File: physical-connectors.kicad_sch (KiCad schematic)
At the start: 2 parts, among them J1 M.2_Key_B

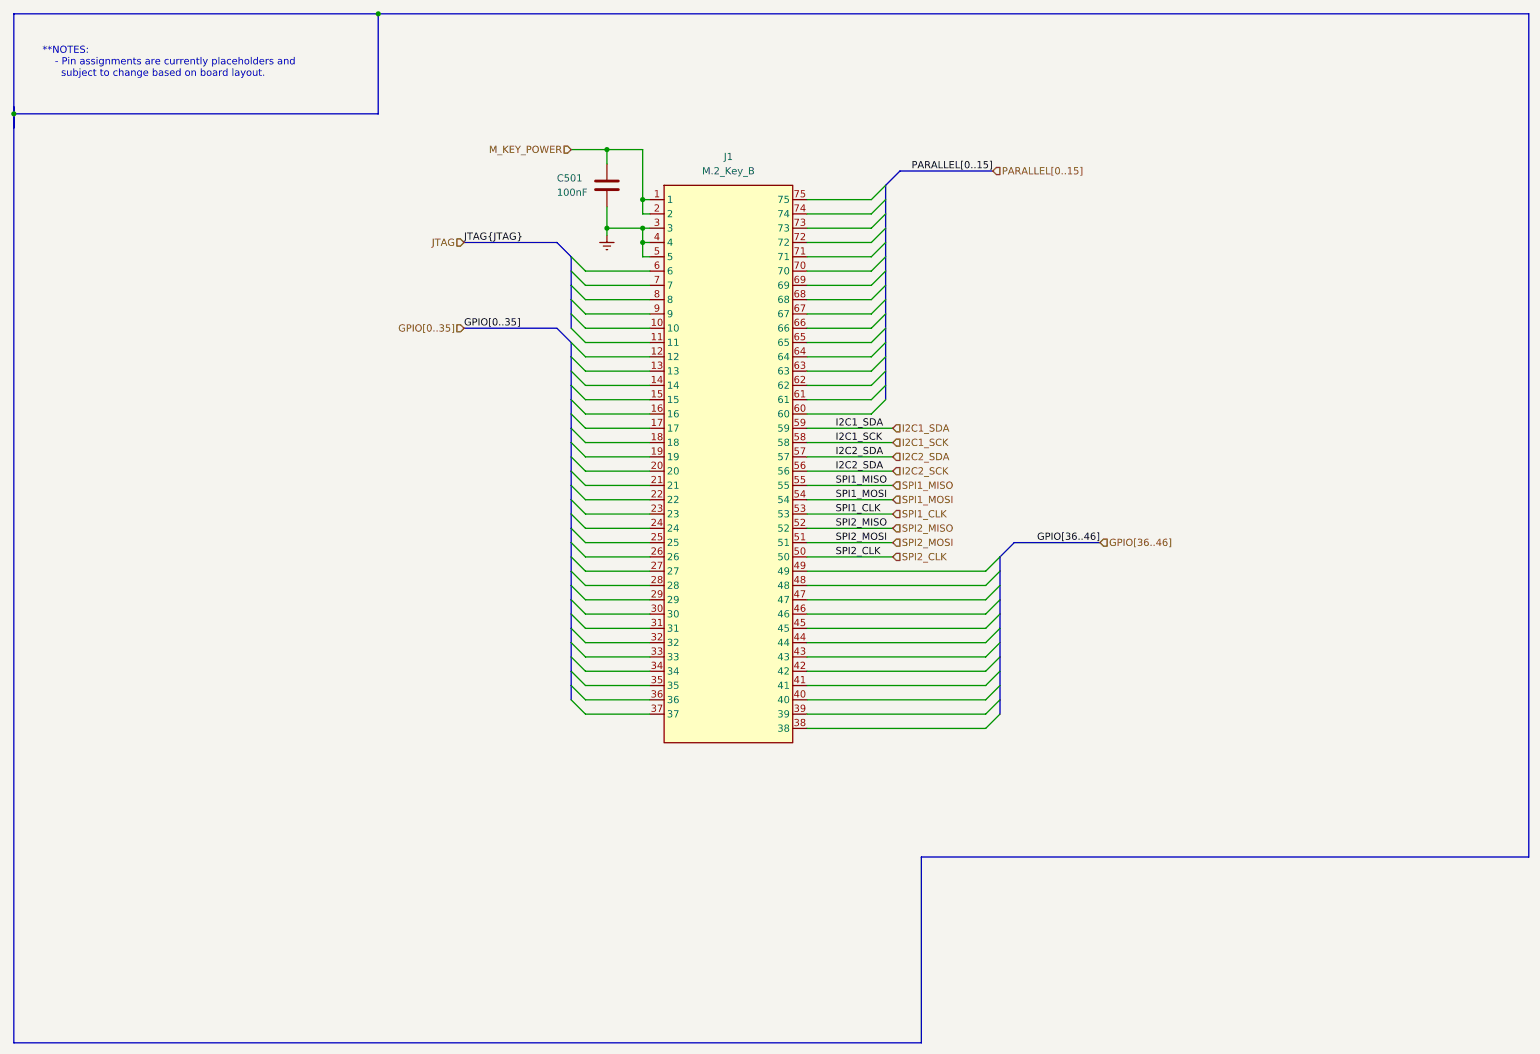
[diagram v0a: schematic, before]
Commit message: added net labels; changed colours
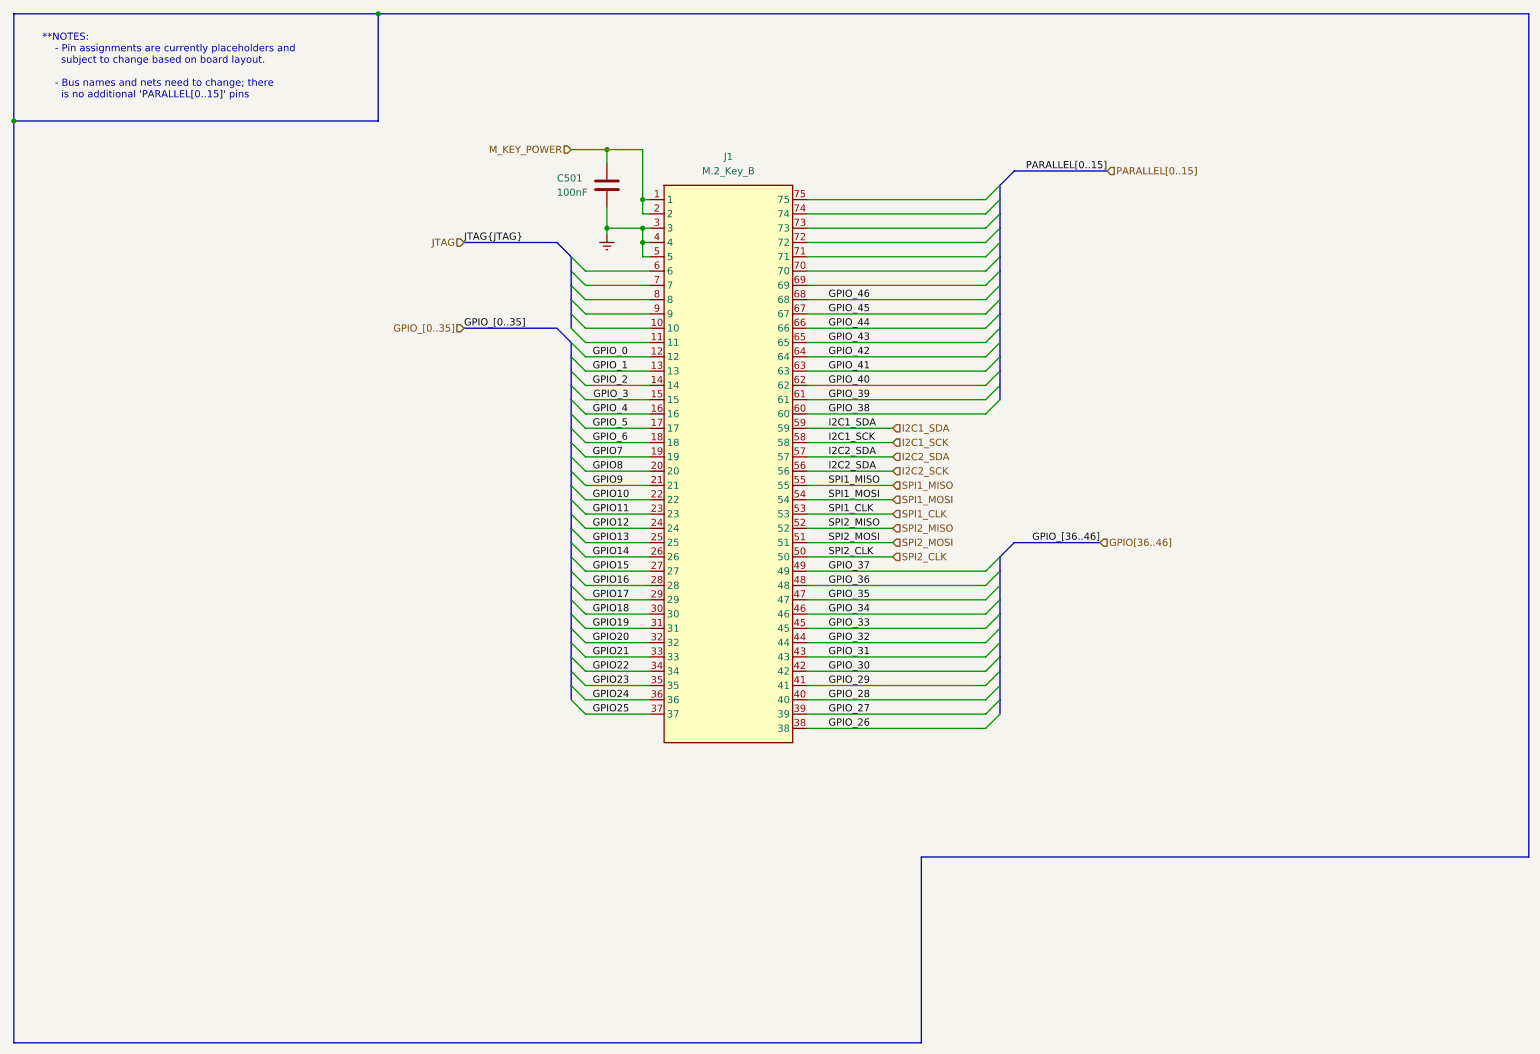
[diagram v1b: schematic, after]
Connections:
- net GPIO_0: now reaches J1.12
- net GPIO_1: now reaches J1.13
- net GPIO_2: now reaches J1.14
- net GPIO_3: now reaches J1.15
- net GPIO_4: now reaches J1.16
- net GPIO_5: now reaches J1.17
- net GPIO_6: now reaches J1.18
- net GPIO7: now reaches J1.19
- net GPIO8: now reaches J1.20
- net GPIO9: now reaches J1.21
- net GPIO10: now reaches J1.22
- net GPIO11: now reaches J1.23
- net GPIO12: now reaches J1.24
- net GPIO13: now reaches J1.25
- net GPIO14: now reaches J1.26
- net GPIO15: now reaches J1.27
- net GPIO16: now reaches J1.28
- net GPIO17: now reaches J1.29
- net GPIO18: now reaches J1.30
- net GPIO19: now reaches J1.31
- net GPIO20: now reaches J1.32
- net GPIO21: now reaches J1.33
- net GPIO22: now reaches J1.34
- net GPIO23: now reaches J1.35
- net GPIO24: now reaches J1.36
- net GPIO25: now reaches J1.37
- net GPIO_26: now reaches J1.38
- net GPIO_27: now reaches J1.39
- net GPIO_28: now reaches J1.40
- net GPIO_29: now reaches J1.41
- net GPIO_30: now reaches J1.42
- net GPIO_31: now reaches J1.43
- net GPIO_32: now reaches J1.44
- net GPIO_33: now reaches J1.45
- net GPIO_34: now reaches J1.46
- net GPIO_35: now reaches J1.47
- net GPIO_36: now reaches J1.48
- net GPIO_37: now reaches J1.49
- net GPIO_38: now reaches J1.60
- net GPIO_39: now reaches J1.61
- net GPIO_40: now reaches J1.62
- net GPIO_41: now reaches J1.63
- net GPIO_42: now reaches J1.64
- net GPIO_43: now reaches J1.65
- net GPIO_44: now reaches J1.66
- net GPIO_45: now reaches J1.67
- net GPIO_46: now reaches J1.68
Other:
- note added: "**NOTES: - Pin assignments are currently placeholders and subject to change based on board layout. - Bus names and nets need to change; there is no additional 'PARALLEL[0..15]' pins"
- note removed: "**NOTES: - Pin assignments are currently placeholders and subject to change based on board layout."
